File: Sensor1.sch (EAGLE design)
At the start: 4 parts

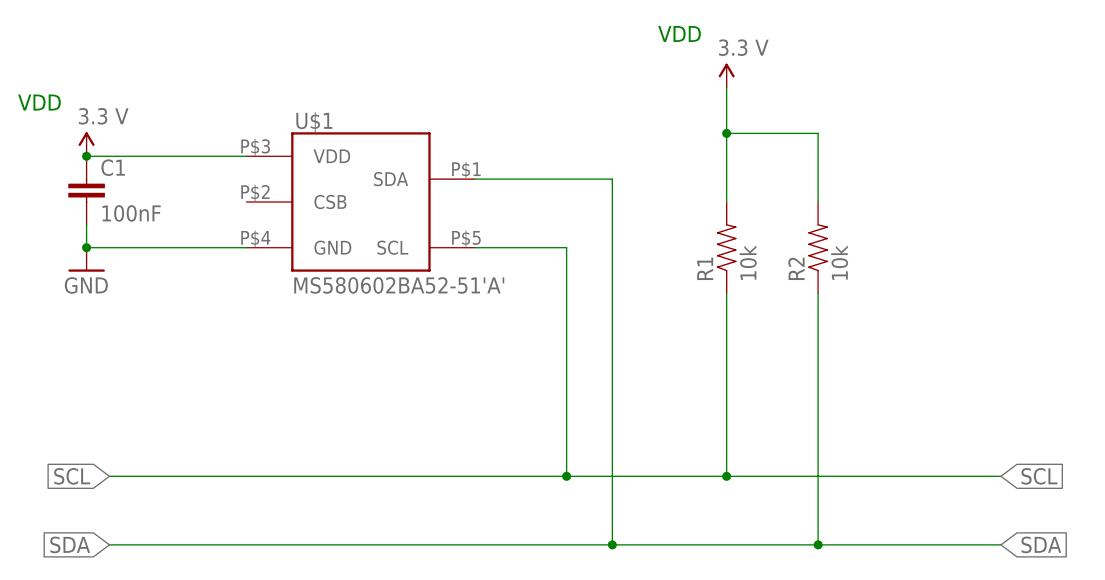
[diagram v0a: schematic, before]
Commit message: Add files via upload
fixed the Schematic
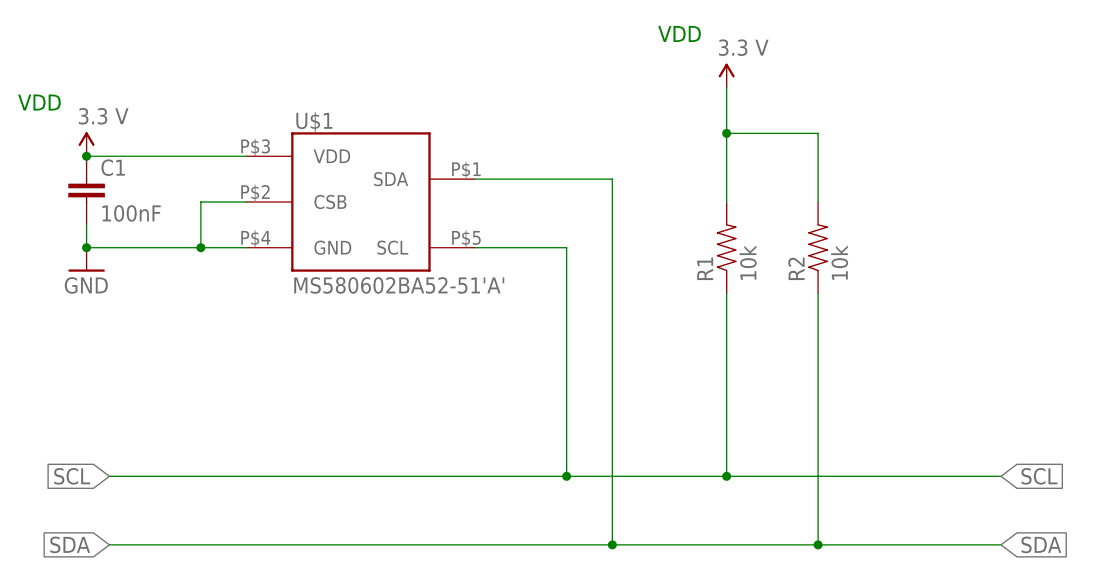
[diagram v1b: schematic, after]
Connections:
- net GND: now also U$1.CSB
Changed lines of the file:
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@@
 <wire x1="-30.48" y1="-2.54" x2="-30.48" y2="-5.08" width="0.1524" layer="91"/>
 <pinref part="U$1" gate="G$1" pin="GND"/>
-<wire x1="-12.7" y1="-5.08" x2="-30.48" y2="-5.08" width="0.1524" layer="91"/>
+<wire x1="-12.7" y1="-5.08" x2="-17.78" y2="-5.08" width="0.1524" layer="91"/>
 <junction x="-30.48" y="-5.08"/>
+<pinref part="U$1" gate="G$1" pin="CSB"/>
+<wire x1="-17.78" y1="-5.08" x2="-30.48" y2="-5.08" width="0.1524" layer="91"/>
+<wire x1="-12.7" y1="0" x2="-17.78" y2="0" width="0.1524" layer="91"/>
+<wire x1="-17.78" y1="0" x2="-17.78" y2="-5.08" width="0.1524" layer="91"/>
+<junction x="-17.78" y="-5.08"/>
 </segment>
 </net>
